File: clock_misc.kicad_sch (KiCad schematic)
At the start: 30 parts, among them J12 SWH, U20 74LVC1G80, U21 FANOUT, U22 74AHC1G14, U23 74AHC1G14, U25 74AHC1G14, Y1 TCXO

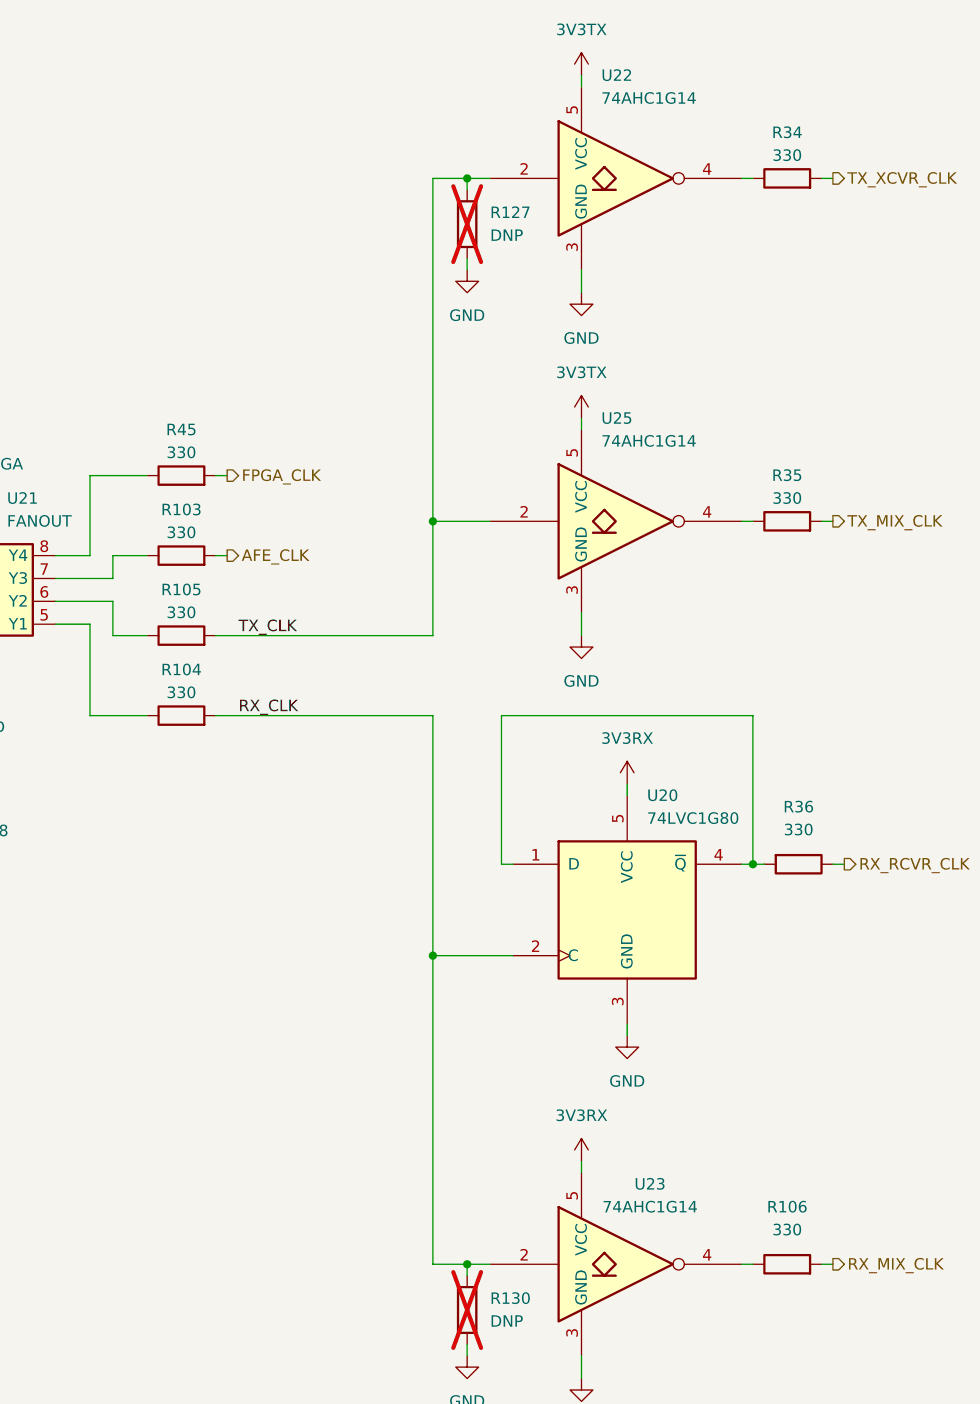
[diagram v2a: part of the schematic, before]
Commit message: Tune clock passives
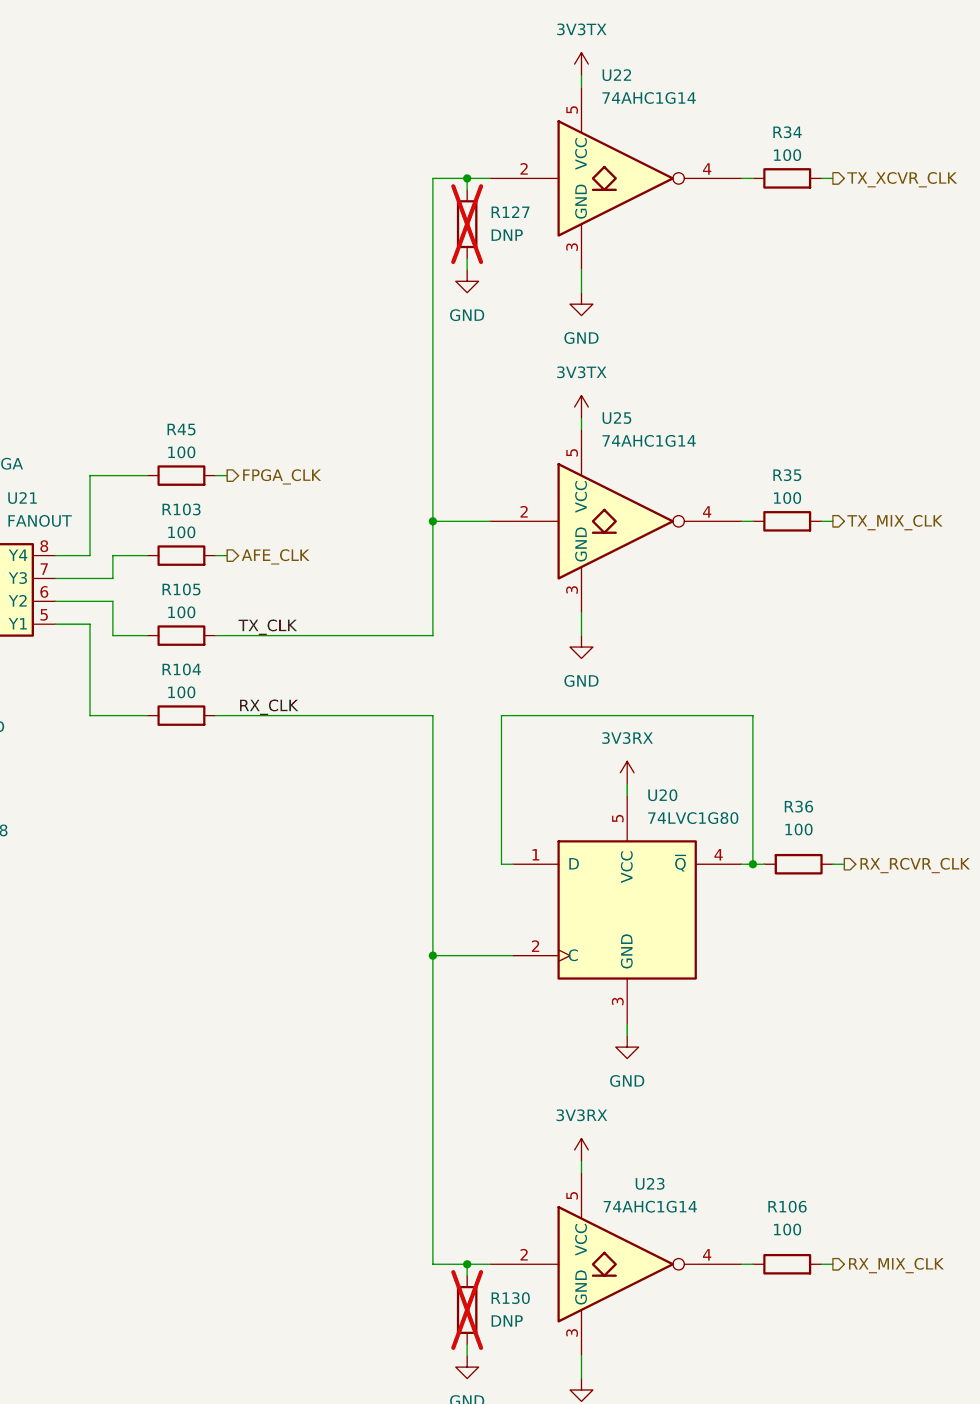
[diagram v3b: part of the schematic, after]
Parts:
- R103, R104, R105, R106, R34, R35, R36, R45: value 330 -> 100; Part Number RC0402FR-13330RL -> RC0402JR-07100RL
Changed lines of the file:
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@@
       (effects (font (size 1.27 1.27)))
     )
-    (property "Value" "330" (at 115.57 85.09 90)
+    (property "Value" "100" (at 115.57 85.09 90)
       (effects (font (size 1.27 1.27)))
     )
@@
       (effects (font (size 1.27 1.27)) hide)
     )
-    (property "Part Number" "RC0402FR-13330RL" (at 115.57 87.63 0)
+    (property "Part Number" "RC0402JR-07100RL" (at 115.57 87.63 0)
       (effects (font (size 1.27 1.27)) hide)
     )
@@
       (effects (font (size 1.27 1.27)) hide)
     )
-    (property "Description" "RES 330 OHM 1% 1/16W 0402" (at 115.57 87.63 0)
+    (property "Description" "RES 100 OHM 5% 1/16W 0402" (at 115.57 87.63 0)
       (effects (font (size 1.27 1.27)) hide)
     )
@@
       (effects (font (size 1.27 1.27)))
     )
-    (property "Value" "330" (at 115.57 67.31 90)
+    (property "Value" "100" (at 115.57 67.31 90)
       (effects (font (size 1.27 1.27)))
     )
@@
       (effects (font (size 1.27 1.27)) hide)
     )
-    (property "Part Number" "RC0402FR-13330RL" (at 115.57 69.85 0)
+    (property "Part Number" "RC0402JR-07100RL" (at 115.57 69.85 0)
       (effects (font (size 1.27 1.27)) hide)
     )
@@
       (effects (font (size 1.27 1.27)) hide)
     )
-    (property "Description" "RES 330 OHM 1% 1/16W 0402" (at 115.57 69.85 0)
+    (property "Description" "RES 100 OHM 5% 1/16W 0402" (at 115.57 69.85 0)
       (effects (font (size 1.27 1.27)) hide)
     )
@@
       (effects (font (size 1.27 1.27)))
     )
-    (property "Value" "330" (at 184.15 109.22 90)
+    (property "Value" "100" (at 184.15 109.22 90)
       (effects (font (size 1.27 1.27)))
     )
@@
       (effects (font (size 1.27 1.27)) hide)
     )
-    (property "Part Number" "RC0402FR-13330RL" (at 184.15 113.03 0)
+    (property "Part Number" "RC0402JR-07100RL" (at 184.15 113.03 0)
       (effects (font (size 1.27 1.27)) hide)
     )
@@
       (effects (font (size 1.27 1.27)) hide)
     )
-    (property "Description" "RES 330 OHM 1% 1/16W 0402" (at 184.15 113.03 0)
+    (property "Description" "RES 100 OHM 5% 1/16W 0402" (at 184.15 113.03 0)
       (effects (font (size 1.27 1.27)) hide)
     )
@@
       (effects (font (size 1.27 1.27)))
     )
-    (property "Value" "330" (at 115.57 93.98 90)
+    (property "Value" "100" (at 115.57 93.98 90)
       (effects (font (size 1.27 1.27)))
     )
@@
       (effects (font (size 1.27 1.27)) hide)
     )
-    (property "Part Number" "RC0402FR-13330RL" (at 115.57 96.52 0)
+    (property "Part Number" "RC0402JR-07100RL" (at 115.57 96.52 0)
       (effects (font (size 1.27 1.27)) hide)
     )
@@
       (effects (font (size 1.27 1.27)) hide)
     )
-    (property "Description" "RES 330 OHM 1% 1/16W 0402" (at 115.57 96.52 0)
+    (property "Description" "RES 100 OHM 5% 1/16W 0402" (at 115.57 96.52 0)
       (effects (font (size 1.27 1.27)) hide)
     )
@@
       (effects (font (size 1.27 1.27)))
     )
-    (property "Value" "330" (at 182.88 72.39 90)
+    (property "Value" "100" (at 182.88 72.39 90)
       (effects (font (size 1.27 1.27)))
     )
@@
       (effects (font (size 1.27 1.27)) hide)
     )
-    (property "Part Number" "RC0402FR-13330RL" (at 182.88 74.93 0)
+    (property "Part Number" "RC0402JR-07100RL" (at 182.88 74.93 0)
       (effects (font (size 1.27 1.27)) hide)
     )
@@
       (effects (font (size 1.27 1.27)) hide)
     )
-    (property "Description" "RES 330 OHM 1% 1/16W 0402" (at 182.88 74.93 0)
+    (property "Description" "RES 100 OHM 5% 1/16W 0402" (at 182.88 74.93 0)
       (effects (font (size 1.27 1.27)) hide)
     )
@@
       (effects (font (size 1.27 1.27)))
     )
-    (property "Value" "330" (at 182.88 34.29 90)
+    (property "Value" "100" (at 182.88 34.29 90)
       (effects (font (size 1.27 1.27)))
     )
@@
       (effects (font (size 1.27 1.27)) hide)
     )
-    (property "Part Number" "RC0402FR-13330RL" (at 182.88 36.83 0)
+    (property "Part Number" "RC0402JR-07100RL" (at 182.88 36.83 0)
       (effects (font (size 1.27 1.27)) hide)
     )
@@
       (effects (font (size 1.27 1.27)) hide)
     )
-    (property "Description" "RES 330 OHM 1% 1/16W 0402" (at 182.88 36.83 0)
+    (property "Description" "RES 100 OHM 5% 1/16W 0402" (at 182.88 36.83 0)
       (effects (font (size 1.27 1.27)) hide)
     )
@@
       (effects (font (size 1.27 1.27)))
     )
-    (property "Value" "330" (at 115.57 76.2 90)
+    (property "Value" "100" (at 115.57 76.2 90)
       (effects (font (size 1.27 1.27)))
     )
@@
       (effects (font (size 1.27 1.27)) hide)
     )
-    (property "Part Number" "RC0402FR-13330RL" (at 115.57 78.74 0)
+    (property "Part Number" "RC0402JR-07100RL" (at 115.57 78.74 0)
       (effects (font (size 1.27 1.27)) hide)
     )
@@
       (effects (font (size 1.27 1.27)) hide)
     )
-    (property "Description" "RES 330 OHM 1% 1/16W 0402" (at 115.57 78.74 0)
+    (property "Description" "RES 100 OHM 5% 1/16W 0402" (at 115.57 78.74 0)
       (effects (font (size 1.27 1.27)) hide)
     )
@@
       (effects (font (size 1.27 1.27)))
     )
-    (property "Value" "330" (at 182.88 153.67 90)
+    (property "Value" "100" (at 182.88 153.67 90)
       (effects (font (size 1.27 1.27)))
     )
@@
       (effects (font (size 1.27 1.27)) hide)
     )
-    (property "Part Number" "RC0402FR-13330RL" (at 182.88 157.48 0)
+    (property "Part Number" "RC0402JR-07100RL" (at 182.88 157.48 0)
       (effects (font (size 1.27 1.27)) hide)
     )
@@
       (effects (font (size 1.27 1.27)) hide)
     )
-    (property "Description" "RES 330 OHM 1% 1/16W 0402" (at 182.88 157.48 0)
-      (effects (font (size 1.27 1.27)) hide)
-    )
+    (property "Description" "RES 100 OHM 5% 1/16W 0402" (at 182.88 157.48 0)
+      (effects (font (size 1.27 1.27)) hide)
+    )
